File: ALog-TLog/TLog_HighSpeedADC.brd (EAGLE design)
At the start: 124.1 x 45.3 mm, 95 parts, among them IC1 ATMEGA644M, J6 5.5x2.1mm Barrel, Q1 220mA/50V/3.5Ω, Q5 4.3A/20V/54mΩ, Q6 4.3A/20V/54mΩ, Q7 4.3A/20V/54mΩ, Q8 220mA/50V/3.5Ω, Q9 220mA/50V/3.5Ω, U2 FT231X-Q, U3 915MHz, U4 SX1509, X2 87832-14

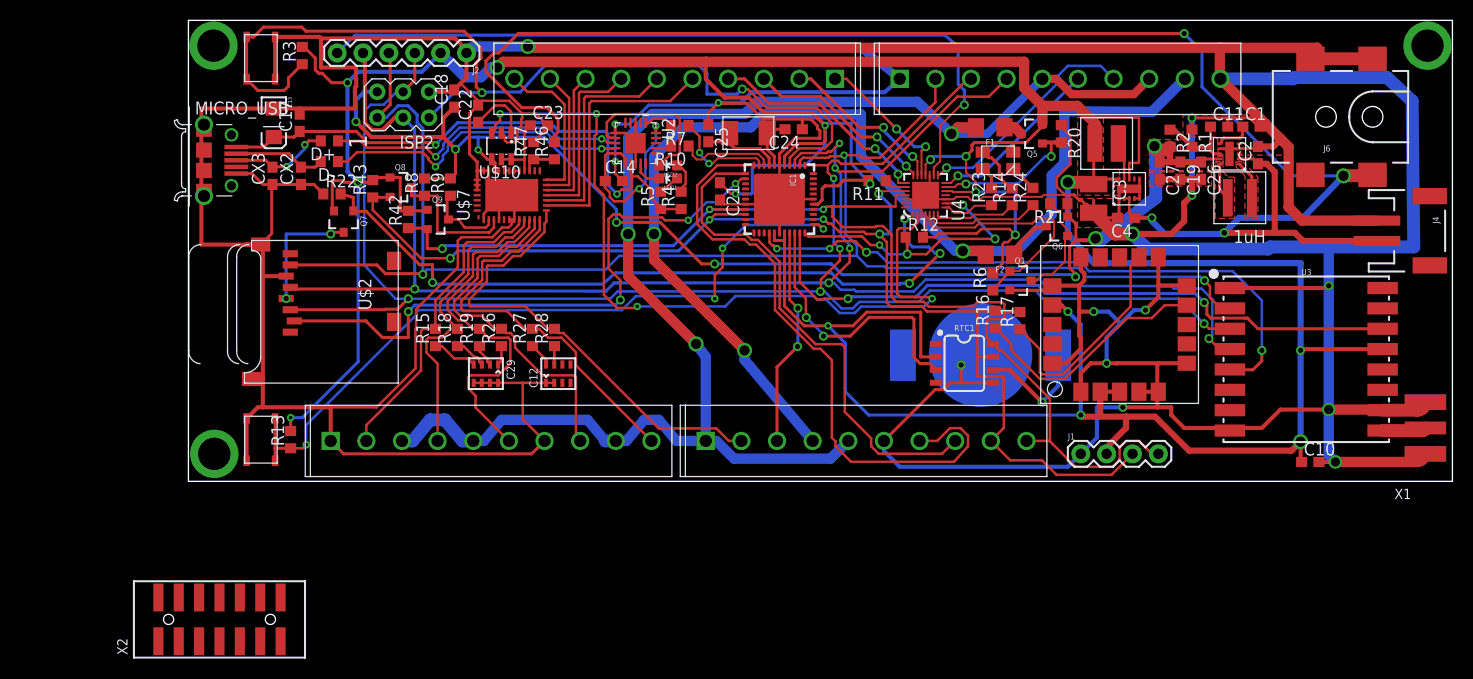
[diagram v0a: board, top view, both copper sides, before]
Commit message: TLog Board Ready for Review
TLog board is at functional stage and ready for review by general eyes, High Speed ADC daughter board preliminary files also added (location may change eventually)
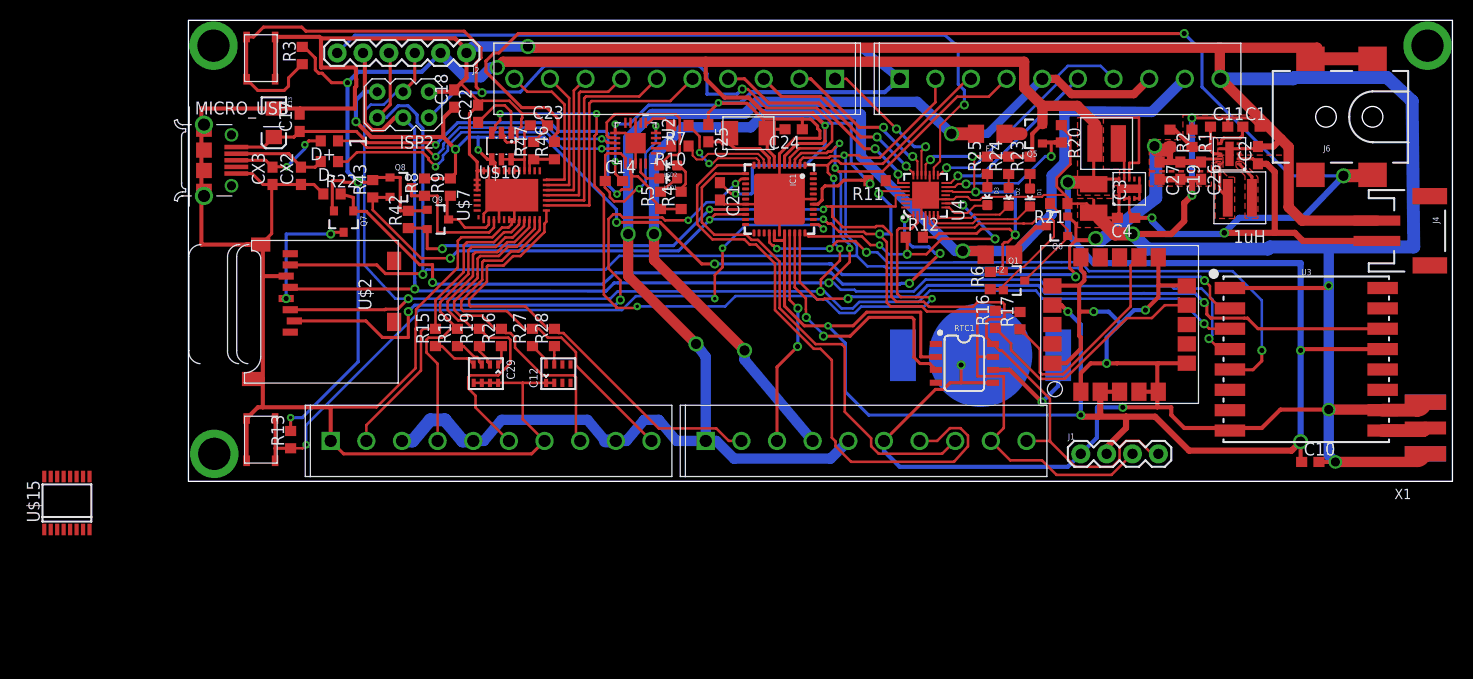
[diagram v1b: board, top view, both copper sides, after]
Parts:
- removed R14: 330, resistor:R0603
- removed X2: 87832-14, con-molex:87832-14
- added D1, D2, D3: (no value), SparkFun-LED:LED-0603
- added R25: 330, rcl:R0603
- R23, R24: device resistor:R0603 -> rcl:R0603
- R6: value (none) -> 10k
- U$15: value CLVBA-FKA -> LTC2440; device bschulz:CLVBA-FKA -> bschulz:SSOP16
- moved U$15 97.4 mm to (-11.8, -2.03), turned to 0 degrees
- moved R23 4.86 mm to (82.8, 31.1)
- moved R24 3.88 mm to (80.7, 31.1)
- moved F1 0.63 mm to (78.9, 34.2)
- moved Q1 0.63 mm to (81.2, 19.8)
- moved R6 0.28 mm to (78.9, 19.8)
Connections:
- removed net 3V3: C10.1, C21.1, C3.1, IC1.17, IC1.27, IC1.29, IC1.38, IC1.5, J1.2, J2.2, L2.P$2, Q5.2, Q7.2, Q8.1, Q9.1, R11.2, R12.2, R13.2, R3.2, R42.2, R43.2, R6.2, RTC1.2, U$15.2, U$4.P$10, U$4.P$8, U$6.17, U$6.2, U$6.3, U3.13, U4.12, U4.18, U4.4
- removed net D1_UNIV: IC1.40, X2.5
- removed net D2_UNIV: IC1.41, X2.14
- removed net N$10: R23.2, U$15.4
- removed net N$15: R24.2, U$15.1
- removed net N$9: R14.2, U$15.3
- new net 3.3V: C10.1, C21.1, C3.1, IC1.17, IC1.27, IC1.29, IC1.38, IC1.5, J1.2, J2.2, L2.P$2, Q1.1, Q5.2, Q7.2, Q8.1, Q9.1, R11.2, R12.2, R13.2, R23.2, R24.2, R25.2, R3.2, R42.2, R43.2, R6.2, RTC1.2, U$4.P$10, U$4.P$8, U$6.17, U$6.2, U$6.3, U3.13, U4.12, U4.18, U4.4
- new net ADC_CS: IC1.25
- new net N$32: D1.A, R23.1
- new net N$33: D2.A, R24.1
- new net N$34: D3.A, R25.1
- net 5V: no longer R21.1
- net 5V_EXT_CTRL: now also Q1.2; no longer Q1.1
- net ADC5: no longer X2.12
- net ADC6: no longer X2.13
- net EXT_3.3V: no longer X2.2
- net EXT_5V: no longer X2.3
- net GND: now also R21.1; no longer Q1.2, X2.1
- net LED1: now also D1.C; no longer R24.1
- net LED2: now also D2.C; no longer R14.1
- net LED3: now also D3.C; no longer R23.1
- net MISO: no longer X2.6
- net MOSI: no longer X2.9
- net RX_EXT: no longer X2.7
- net SCK: no longer X2.10
- net SCL: no longer X2.11
- net SDA: no longer X2.4
- net TX_EXT: no longer X2.8
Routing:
- net 3.3V: track 0.00 -> 434.8 mm, vias 0 -> 17
- net 3V3: track 432.3 -> 0.00 mm, vias 17 -> 0
- net GND: track 806.5 -> 801.5 mm
- net N$9: track 5.02 -> 0.00 mm
- net N$15: track 2.72 -> 0.00 mm
- net N$10: track 2.26 -> 0.00 mm
- net N$32: track 0.00 -> 1.43 mm
- net N$33: track 0.00 -> 1.37 mm
- net N$34: track 0.00 -> 1.31 mm
- net 5V: track 128.9 -> 127.6 mm
- net N$30: track 10.7 -> 10.0 mm
- added copper zone on layer 1, net 3.3V
- removed copper zone on layer 1, net 3V3
